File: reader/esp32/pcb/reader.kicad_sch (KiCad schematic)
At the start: 12 parts, among them U1 ESP32-WROOM-32U, U2 RDM6300

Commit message: Work.
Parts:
- added C2, C3: C, symbol Device:C
- added J1: Conn_01x06, Connector_USB:USB_Micro-B_Molex-105017-0001, symbol Connector_Generic:Conn_01x06
- added Q1, Q2: MMBT3904, Package_TO_SOT_SMD:SOT-23, symbol Device:Q_NPN_BEC
- added R5, R6: 10K, symbol Device:R
- added U3: CH340C, Package_SO:SOIC-16_3.9x9.9mm_P1.27mm, symbol Interface_USB:CH340C
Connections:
- net +5V: now also C3.1, J1.1 (Pin_1), U3.16 (VCC)
- net GND: now also C2.2, C3.2, J1.5 (Pin_5), J1.6 (Pin_6), U3.1 (GND)
- net IO0: now reaches U1.25 (IO0)
- net IO0: now also Q2.3 (C)
- net EN: now reaches U1.3 (EN)
- net EN: now also Q1.3 (C)
- net SENSE: now reaches R3.2, R4.1
- new net: Q1.2 (E), R6.1, U3.14 (~RTS)
- new net: Q2.1 (B), R6.2
- new net: C2.1, U3.4 (V3)
- new net: J1.2 (Pin_2), U3.6 (UD-)
- new net: J1.3 (Pin_3), U3.5 (UD+)
- new net: Q2.2 (E), R5.1, U3.13 (~DTR)
- new net: Q1.1 (B), R5.2
- new net RX: U3.3 (RXD)
- new net TX: U3.2 (TXD)
- no-connect marks 31 -> 10
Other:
- note removed: "Input only"
- moved on the sheet: U1

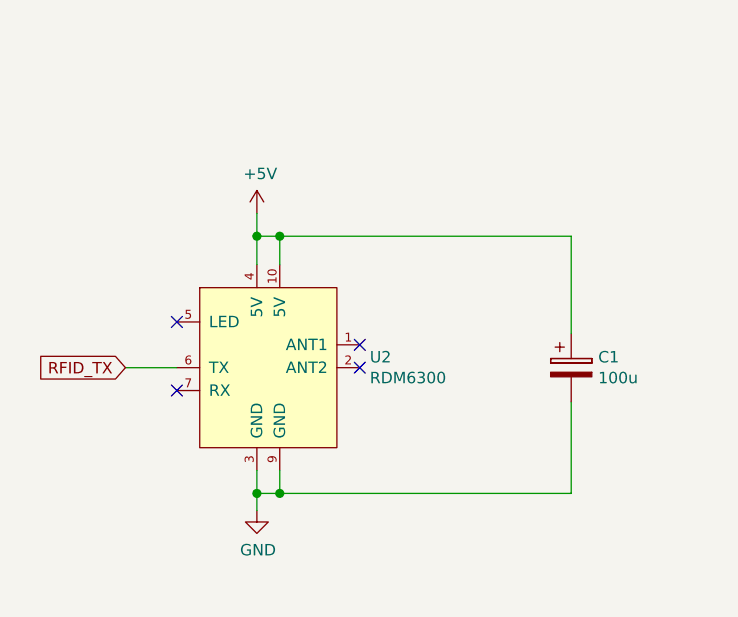
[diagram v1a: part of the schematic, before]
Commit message: Add RF125-PS.
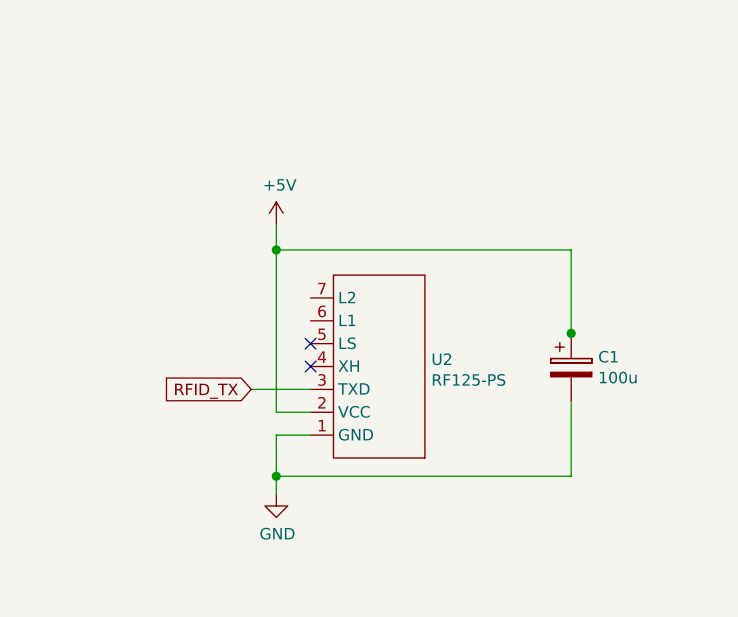
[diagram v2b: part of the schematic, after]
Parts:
- removed U2: RDM6300, Module:RDM6300_B38.5x18.2mm, symbol gtrzps:RDM6300
- added U2: RF125-PS, Module:rf125ps, symbol rf125ps:RF125-PS
- C1: footprint Capacitor_THT:CP_Radial_D6.3mm_P2.50mm -> (none)
- C2, C3: footprint (none) -> Capacitor_SMD:C_0603_1608Metric
- R1, R2, R3, R4: footprint Resistor_SMD:R_0805_2012Metric_Pad1.15x1.40mm_HandSolder -> Resistor_SMD:R_0603_1608Metric
- R5, R6: footprint (none) -> Resistor_SMD:R_0603_1608Metric
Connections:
- net +5V: now also U2.2 (VCC)
- net GND: now also U2.1 (GND); no longer C1.2
- net RFID_TX: now also U2.3 (TXD)
- no-connect marks 10 -> 8

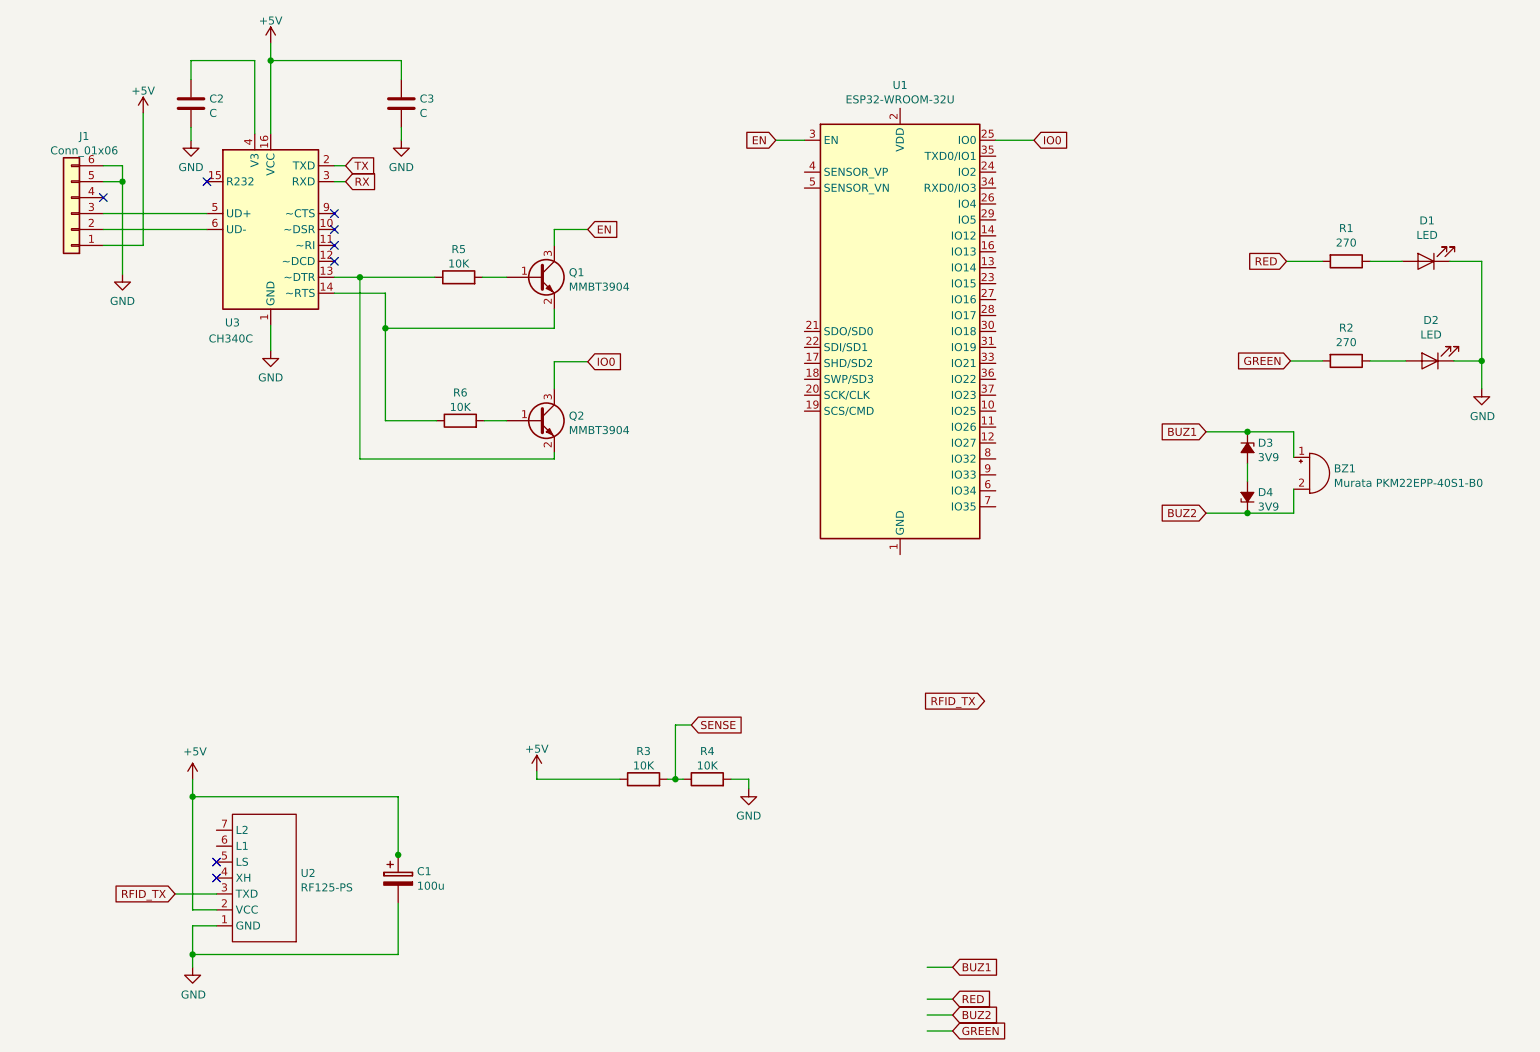
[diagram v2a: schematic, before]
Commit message: Add level converter, regulator.
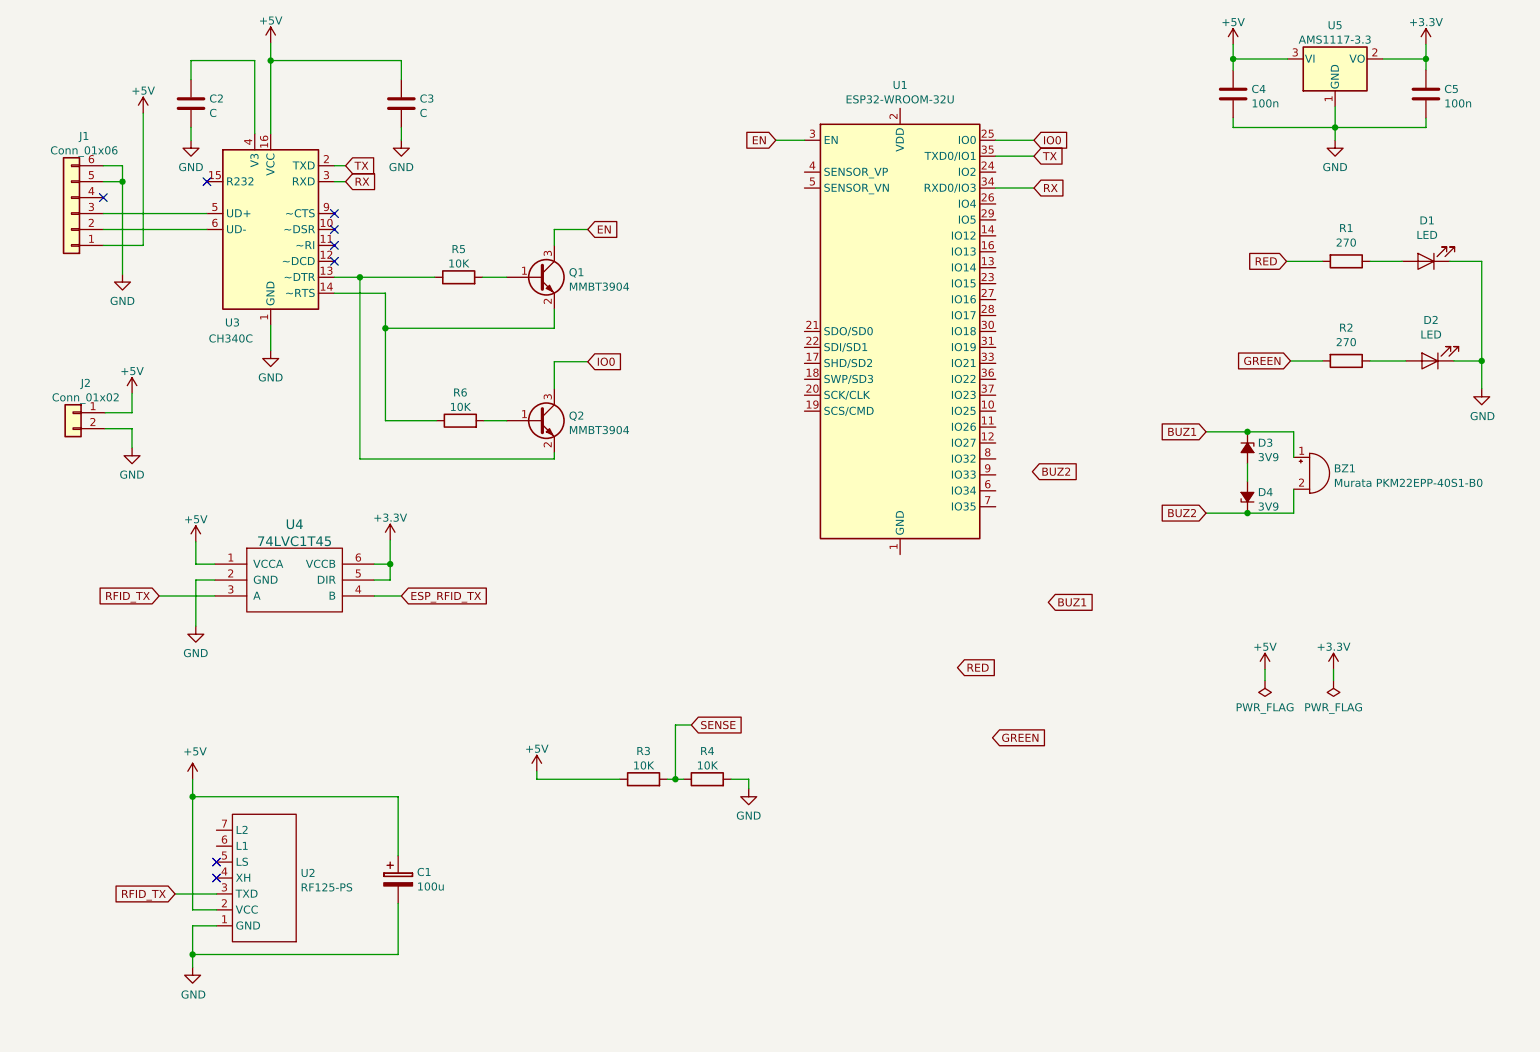
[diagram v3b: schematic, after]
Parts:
- added C4, C5: 100n, symbol Device:C
- added J2: Conn_01x02, symbol Connector_Generic:Conn_01x02
- added U4: 74LVC1T45, symbol 74lvc:74LVC1T45
- added U5: AMS1117-3.3, Package_TO_SOT_SMD:SOT-223-3_TabPin2, symbol Regulator_Linear:AMS1117-3.3
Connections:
- net +5V: now also C4.1, J2.1 (Pin_1), U4.1 (VCCA), U5.3 (VI)
- net GND: now also C1.2, C4.2, C5.2, J2.2 (Pin_2), U4.2 (GND), U5.1 (GND)
- net RFID_TX: now also U4.3 (A)
- net RX: now also U1.34 (RXD0/IO3)
- net TX: now also U1.35 (TXD0/IO1)
- new net +3V3: C5.1, U4.5 (DIR), U4.6 (VCCB), U5.2 (VO)
- new net ESP_RFID_TX: U4.4 (B)

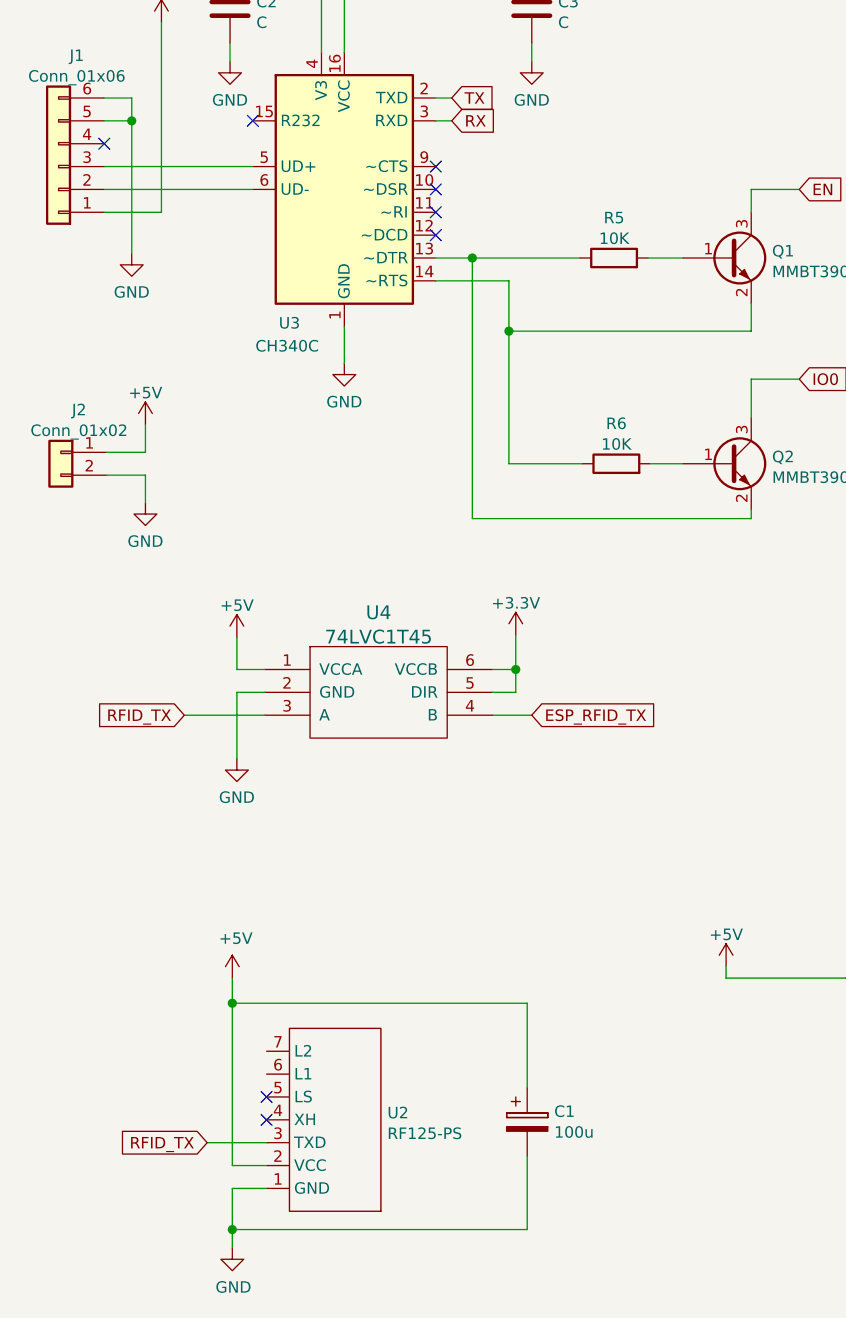
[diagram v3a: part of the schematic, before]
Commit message: Add 4-pin USB connector.
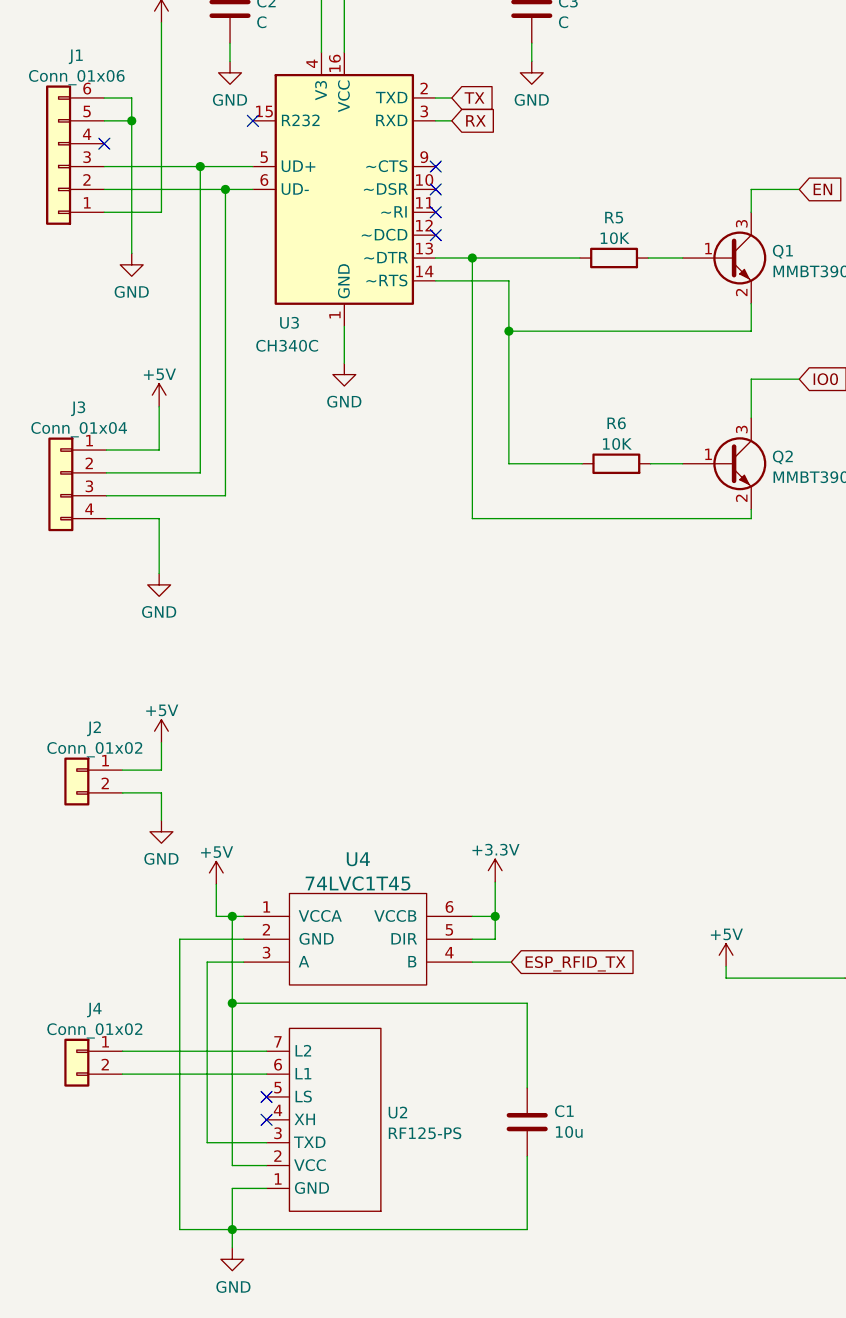
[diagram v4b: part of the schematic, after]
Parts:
- added J3: Conn_01x04, Connector_JST:JST_PH_B4B-PH-K_1x04_P2.00mm_Vertical, symbol Connector_Generic:Conn_01x04
- added J4: Conn_01x02, Connector_JST:JST_XH_B02B-XH-A_1x02_P2.50mm_Vertical, symbol Connector_Generic:Conn_01x02
- C1: value 100u -> 10u; symbol Device:CP -> Device:C
- J2: footprint (none) -> Connector_JST:JST_XH_B02B-XH-A_1x02_P2.50mm_Vertical
- U4: footprint (none) -> Package_TO_SOT_SMD:SOT-363_SC-70-6
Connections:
- net +5V: now also J3.1 (Pin_1)
- net GND: now also J3.4 (Pin_4)
- net at J1.2 (Pin_2), U3.6 (UD-): now also J3.3 (Pin_3)
- net at J1.3 (Pin_3), U3.5 (UD+): now also J3.2 (Pin_2)
- net at U2.6 (L1): now also J4.2 (Pin_2)
- net at U2.7 (L2): now also J4.1 (Pin_1)
- net RFID_TX: no longer names the net of U2.3 (TXD), U4.3 (A)
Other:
- moved on the sheet: J2, U4

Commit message: Fix footprints.
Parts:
- added R7: 100, Resistor_SMD:R_0603_1608Metric, symbol Device:R
- C1: footprint (none) -> Capacitor_SMD:C_0805_2012Metric
- C4, C5: footprint (none) -> Capacitor_SMD:C_0603_1608Metric
- D3, D4: footprint Diode_THT:D_A-405_P7.62mm_Horizontal -> Diode_SMD:D_MiniMELF
- J2: footprint Connector_JST:JST_XH_B02B-XH-A_1x02_P2.50mm_Vertical -> Connector_JST:JST_XH_S02B-XH-A-1_1x02_P2.50mm_Horizontal
- J4: footprint Connector_JST:JST_XH_B02B-XH-A_1x02_P2.50mm_Vertical -> Connector_PinHeader_2.54mm:PinHeader_1x02_P2.54mm_Vertical
- U1: footprint RF_Module:ESP32-WROOM-32U -> RF_Module:ESP32-WROOM-32
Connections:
- net +3V3: now also U1.2 (VDD)
- net BUZ1: now also U1.26 (IO4), R7.1; no longer BZ1.1 (-), D3.1 (K)
- net BUZ2: now also U1.29 (IO5)
- net ESP_RFID_TX: now also U1.30 (IO18)
- net GND: now also U1.1 (GND), U1.15 (GND), U1.38 (GND), U1.39 (GND)
- net GREEN: now also U1.13 (IO14)
- net RED: now also U1.16 (IO13)
- net SENSE: now also U1.8 (IO32)
- new net: BZ1.1 (-), D3.1 (K), R7.2
- no-connect marks 8 -> 11

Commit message: Finish routing.
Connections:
- net BUZ1: now also U1.29 (IO5); no longer U1.26 (IO4)
- net BUZ2: now also U1.26 (IO4); no longer U1.29 (IO5)
- net GREEN: now also U1.16 (IO13); no longer U1.13 (IO14)
- net RED: now also U1.13 (IO14); no longer U1.16 (IO13)
- no-connect marks 11 -> 31
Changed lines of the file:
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@@
   (no_connect (at 66.04 68.58))
   (no_connect (at 66.04 71.12))
+  (no_connect (at 140.97 56.896))
+  (no_connect (at 140.97 59.436))
+  (no_connect (at 140.97 82.296))
+  (no_connect (at 140.97 84.836))
+  (no_connect (at 140.97 87.376))
+  (no_connect (at 140.97 89.916))
+  (no_connect (at 140.97 92.456))
+  (no_connect (at 140.97 94.996))
+  (no_connect (at 171.45 56.896))
   (no_connect (at 171.45 67.056))
+  (no_connect (at 171.45 74.676))
+  (no_connect (at 171.45 77.216))
+  (no_connect (at 171.45 79.756))
+  (no_connect (at 171.45 84.836))
+  (no_connect (at 171.45 87.376))
+  (no_connect (at 171.45 89.916))
+  (no_connect (at 171.45 92.456))
+  (no_connect (at 171.45 94.996))
+  (no_connect (at 171.45 97.536))
+  (no_connect (at 171.45 100.076))
+  (no_connect (at 171.45 105.156))
   (no_connect (at 171.45 107.696))
   (no_connect (at 171.45 110.236))
@@
     )
   )
-  (global_label "BUZ1" (shape input) (at 177.546 61.976 0) (fields_autoplaced)
-    (effects (font (size 1.27 1.27)) (justify left))
-    (property "Intersheet References" "${INTERSHEET_REFS}" (id 0) (at 209.931 -38.989 0)
-      (effects (font (size 1.27 1.27)) (justify left) hide)
-    )
-  )
-  (global_label "BUZ2" (shape input) (at 177.546 64.516 0) (fields_autoplaced)
-    (effects (font (size 1.27 1.27)) (justify left))
-    (property "Intersheet References" "${INTERSHEET_REFS}" (id 0) (at 209.931 -38.989 0)
-      (effects (font (size 1.27 1.27)) (justify left) hide)
-    )
-  )
-  (global_label "RED" (shape input) (at 177.8 69.596 0) (fields_autoplaced)
-    (effects (font (size 1.27 1.27)) (justify left))
-    (property "Intersheet References" "${INTERSHEET_REFS}" (id 0) (at 209.55 -26.289 0)
-      (effects (font (size 1.27 1.27)) (justify left) hide)
-    )
-  )
-  (global_label "GREEN" (shape input) (at 177.8 72.136 0) (fields_autoplaced)
-    (effects (font (size 1.27 1.27)) (justify left))
-    (property "Intersheet References" "${INTERSHEET_REFS}" (id 0) (at 210.185 -26.289 0)
+  (global_label "BUZ2" (shape input) (at 177.546 61.976 0) (fields_autoplaced)
+    (effects (font (size 1.27 1.27)) (justify left))
+    (property "Intersheet References" "${INTERSHEET_REFS}" (id 0) (at 209.931 -41.529 0)
+      (effects (font (size 1.27 1.27)) (justify left) hide)
+    )
+  )
+  (global_label "BUZ1" (shape input) (at 177.546 64.516 0) (fields_autoplaced)
+    (effects (font (size 1.27 1.27)) (justify left))
+    (property "Intersheet References" "${INTERSHEET_REFS}" (id 0) (at 209.931 -36.449 0)
+      (effects (font (size 1.27 1.27)) (justify left) hide)
+    )
+  )
+  (global_label "GREEN" (shape input) (at 177.8 69.596 0) (fields_autoplaced)
+    (effects (font (size 1.27 1.27)) (justify left))
+    (property "Intersheet References" "${INTERSHEET_REFS}" (id 0) (at 210.185 -28.829 0)
+      (effects (font (size 1.27 1.27)) (justify left) hide)
+    )
+  )
+  (global_label "RED" (shape input) (at 177.8 72.136 0) (fields_autoplaced)
+    (effects (font (size 1.27 1.27)) (justify left))
+    (property "Intersheet References" "${INTERSHEET_REFS}" (id 0) (at 209.55 -23.749 0)
       (effects (font (size 1.27 1.27)) (justify left) hide)
     )
@@
     (pin "1")
   )
-  (symbol (lib_name "power:+3.3V_1") (lib_id "power:+3.3V") (at 72.644 143.002 0) (unit 1)
+  (symbol (lib_id "power:+3.3V") (at 72.644 143.002 0) (unit 1)
     (in_bom yes) (on_board yes) (fields_autoplaced)
     (property "Reference" "#PWR014" (id 0) (at 72.644 146.812 0)

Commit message: Fix footprint for 74LVC1T45.
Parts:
- U4: footprint Package_TO_SOT_SMD:SOT-363_SC-70-6 -> Package_TO_SOT_SMD:SOT-23-6
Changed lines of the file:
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@@
       (effects (font (size 1.524 1.524)))
     )
-    (property "Footprint" "Package_TO_SOT_SMD:SOT-363_SC-70-6" (id 2) (at 57.404 149.352 0)
+    (property "Footprint" "Package_TO_SOT_SMD:SOT-23-6" (id 2) (at 57.404 149.352 0)
       (effects (font (size 1.524 1.524)) hide)
     )
@@
     )
     (path "/c43e21ca-2ca8-4e08-a055-c115b36bb4b5"
-      (reference "U4") (unit 1) (value "74LVC1T45") (footprint "Package_TO_SOT_SMD:SOT-363_SC-70-6")
+      (reference "U4") (unit 1) (value "74LVC1T45") (footprint "Package_TO_SOT_SMD:SOT-23-6")
     )
     (path "/b224048b-4b7b-41ed-93cf-7b7ec34b3b4f"
